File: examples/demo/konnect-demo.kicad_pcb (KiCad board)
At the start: 60 x 45 mm, 0 parts

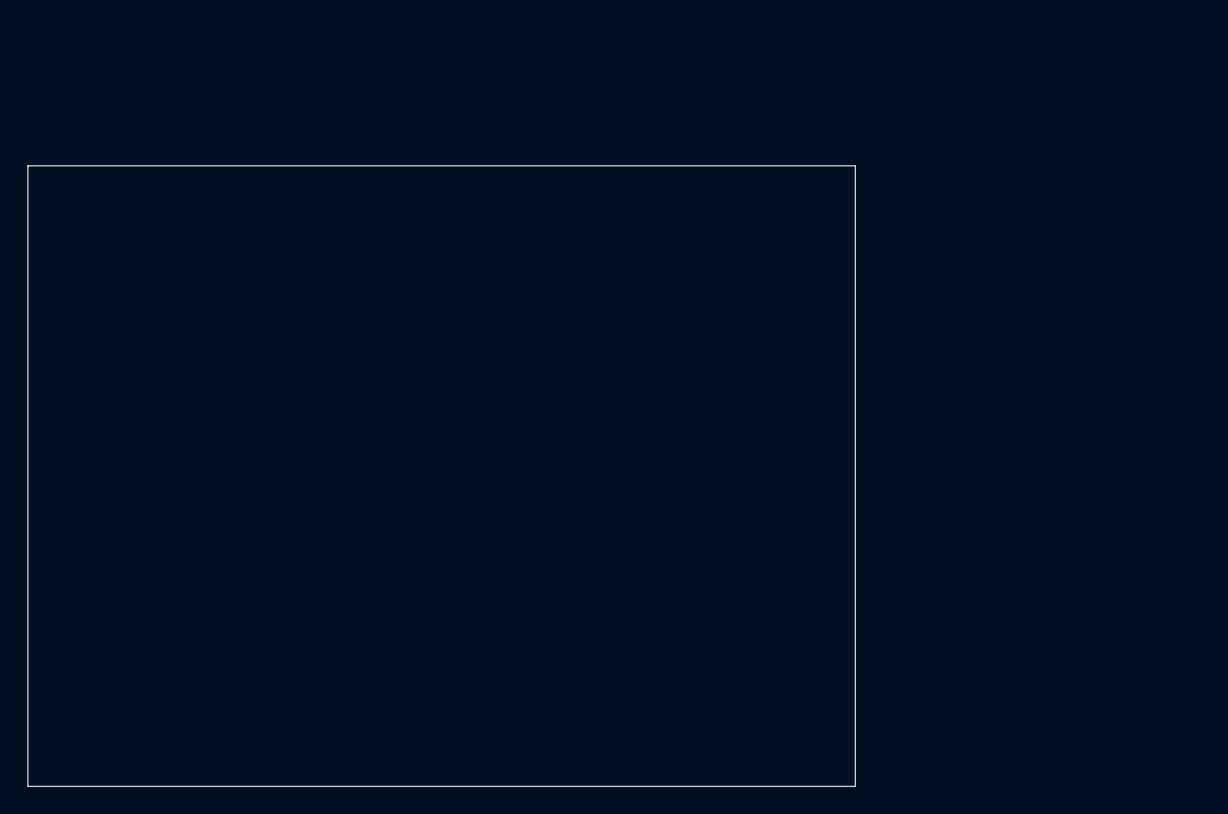
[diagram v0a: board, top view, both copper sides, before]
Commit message: R.3.8: the demo's pre-state carries its own netlist, because nets come from a schematic
Run 1 asked a board with no netlist to be routed. That is a closed path, not a
slow one, so the task changes and the pre-state changes with it.

examples/demo/ is now a real project: a schematic with U1 AP1117-33, C1 and C2
10uF, footprints assigned, VIN/VOUT/GND labelled, two PWR_FLAGs - ERC 0 errors,
0 warnings - pushed onto a 60x45 mm board once through KiCad's own Update PCB
from Schematic. The board therefore starts the way a real layout starts: three
footprints in a heap, five missing connections, and three real nets to close
them with.

The task becomes what a layout engineer does with that heap - place the two
capacitors by the regulator, route the three nets, DRC - which is one batched
kicad_invoke and a check, inside the four turns run 1 measured the 40 s budget
to be worth.

The README states the cost rather than hiding it: a PCB has nets only because a
schematic gave it some, and Update PCB from Schematic is available only when
pcbnew was launched from the project manager - Konnect has no equivalent, so
that step is setup, not demo.

R.3.1's justification is amended, not rewritten: the rejected candidates are
still rejected for the same reasons, and the live PCB edit is still the only
path where KiCad itself redraws.

Co-Authored-By: Claude Opus 5 <noreply@anthropic.com>
Claude-Session: https://claude.ai/code/session_01J2xAkpfUHcT9nWhvxoFQ1S
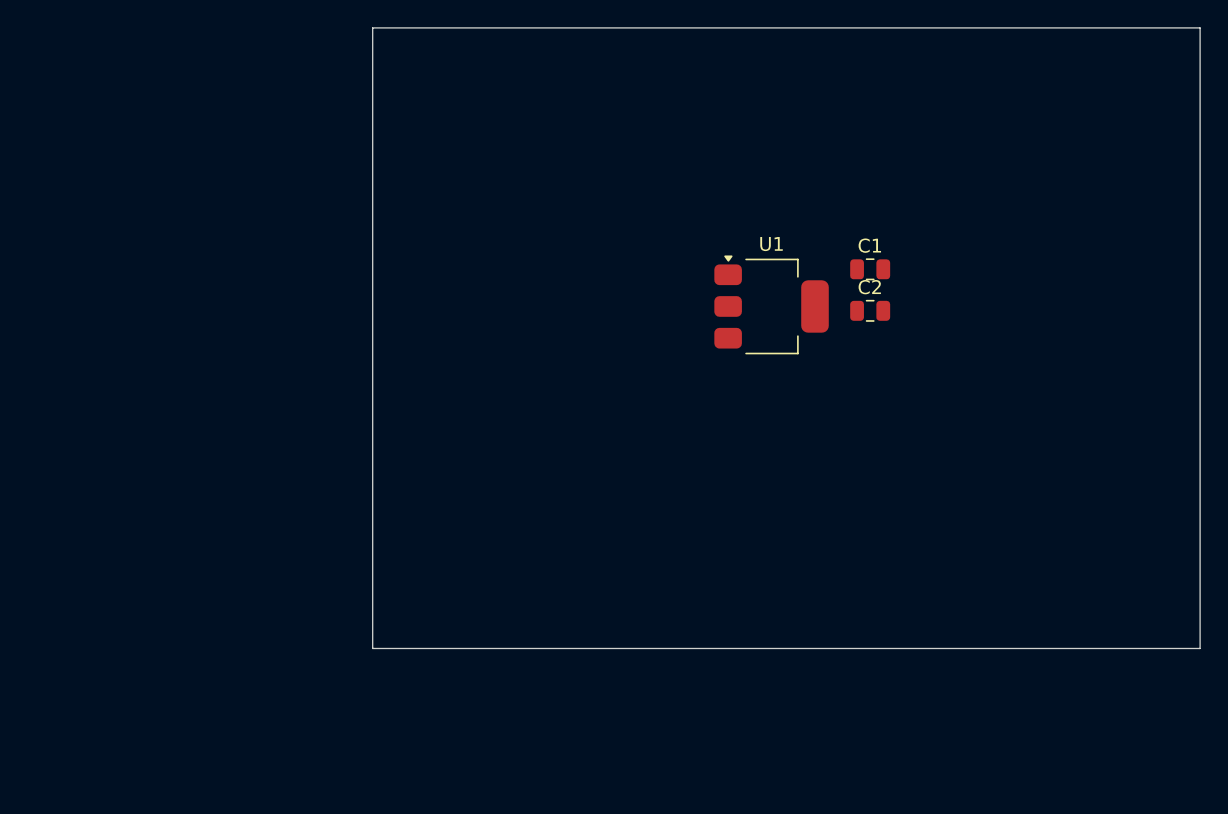
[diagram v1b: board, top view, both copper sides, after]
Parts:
- added C1: 10uF, Capacitor_SMD:C_0805_2012Metric, F.Cu at (161.1, 87.5)
- added C2: 10uF, Capacitor_SMD:C_0805_2012Metric, F.Cu at (161.1, 90.5)
- added U1: AP1117-33, Package_TO_SOT_SMD:SOT-223-3_TabPin2, F.Cu at (153.9, 90.2)
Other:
- copper layers 0 -> 2
